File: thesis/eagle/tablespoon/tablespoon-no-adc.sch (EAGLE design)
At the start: 29 parts, among them IC1 7805DT, IC2 7805DT, IC3 TL072D, U1 ADCS7477, U2 ADCS7477

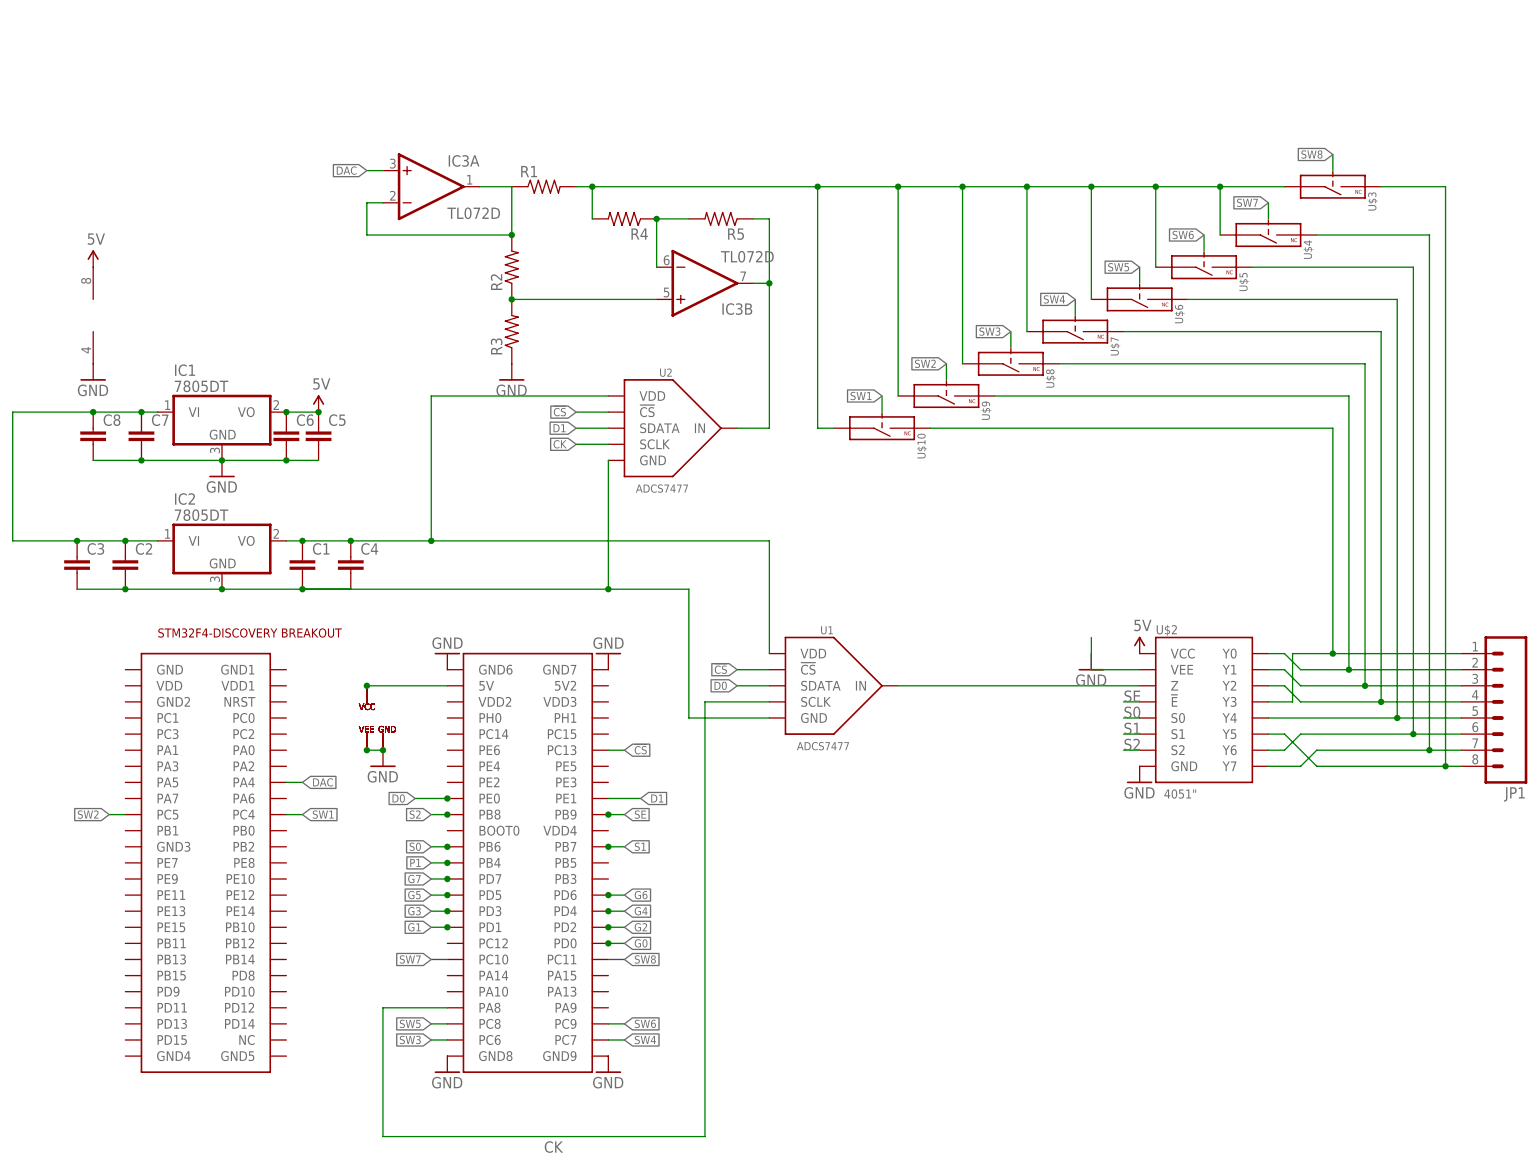
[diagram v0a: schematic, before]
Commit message: working on 8-channel DAC side
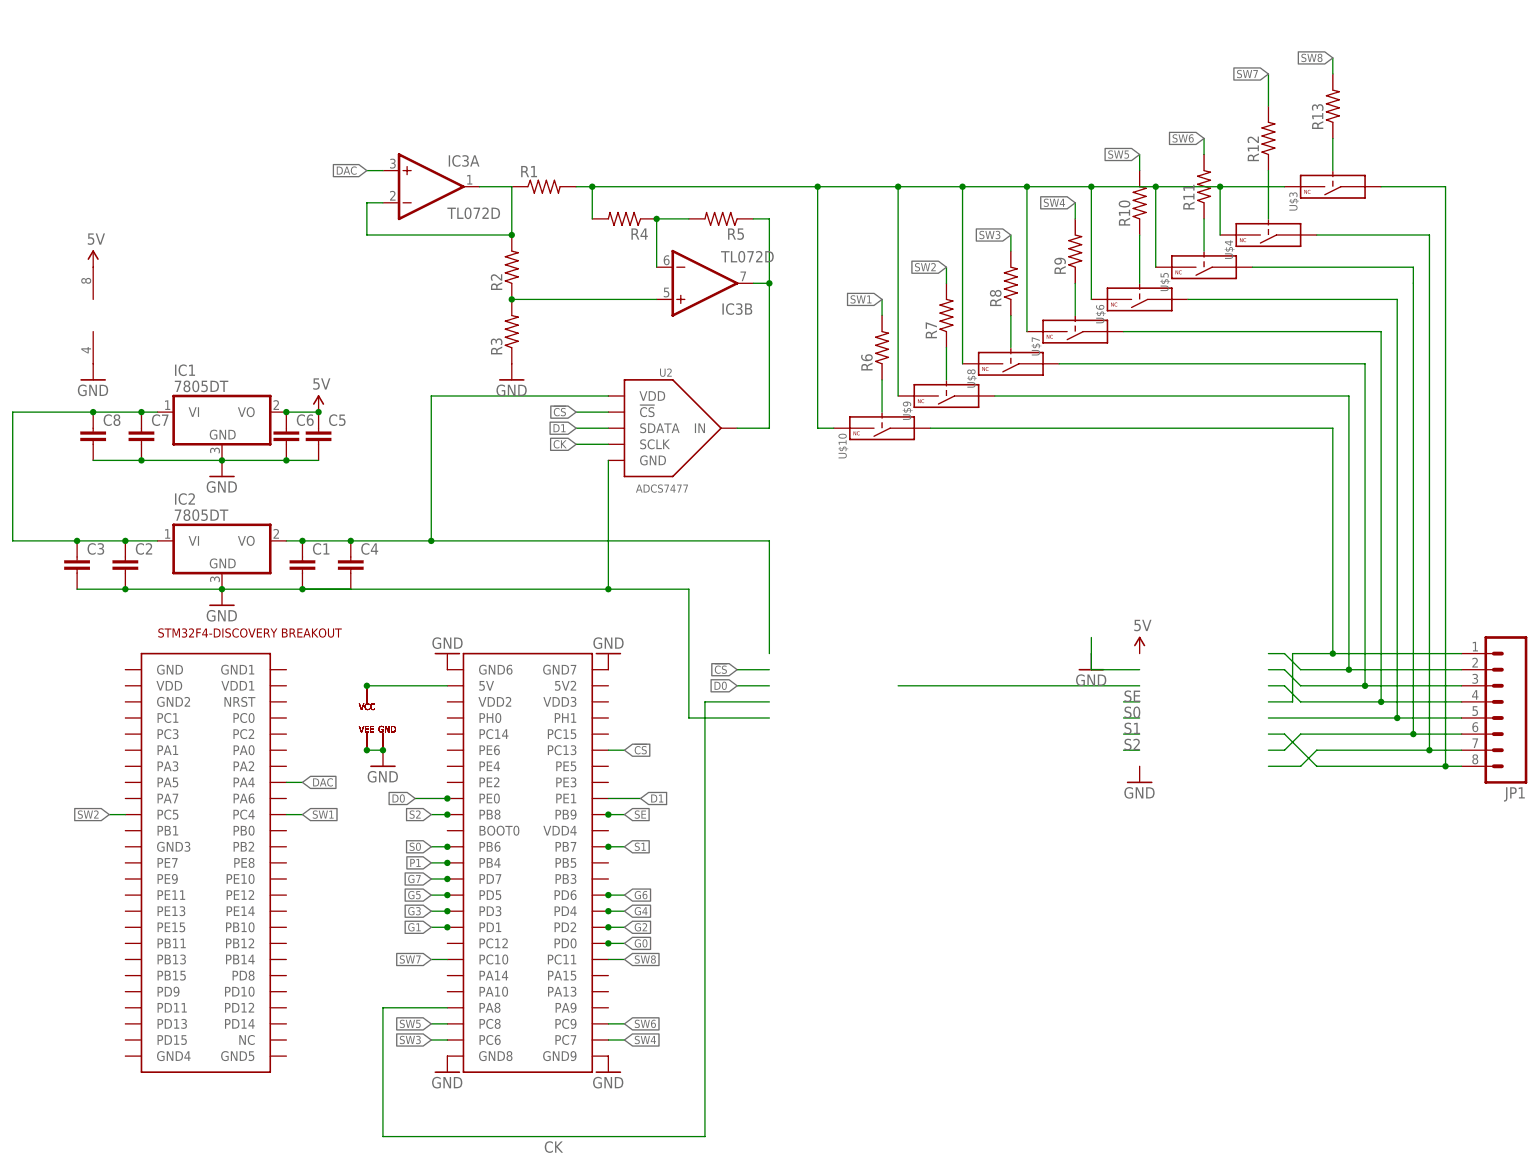
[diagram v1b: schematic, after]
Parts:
- removed U$2: 4051", butter:4051"
- removed U1: ADCS7477, butter:ADCS7477
- added R10, R11, R12, R13, R6, R7, R8, R9: (no value), SparkFun-Passives:RESISTOR0805-RES
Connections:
- net N$7 renamed 4.6V
- removed net N$1: U$2.Z, U1.IN
- removed net N$3: C1.2, C2.2, C3.2, C4.2, IC2.GND, U1.GND, U2.GND
- new net N$15: R8.1, U$8G$1.CTL
- new net N$17: R9.1, U$7G$1.CTL
- new net N$18: R12.1, U$4G$1.CTL
- new net N$19: R13.1, U$3G$1.CTL
- new net N$20: R11.1, U$5G$1.CTL
- new net N$21: R10.1, U$6G$1.CTL
- new net N$4: R6.1, U$10G$1.CTL
- new net N$7: R7.1, U$9G$1.CTL
- net !CS: no longer U1.!CS
- net 5V: no longer U$2.VCC
- net CK: no longer U1.SCLK
- net D0: no longer U1.SDATA
- net GND: now also C1.2, C2.2, C3.2, C4.2, IC2.GND, U2.GND; no longer U$2.GND, U$2.VEE
- net N$10: now also U$8G$1.COM; no longer U$2.Y1, U$8G$1.IN
- net N$11: now also U$10G$1.COM; no longer U$10G$1.IN, U$2.Y3
- net N$12: now also U$9G$1.COM; no longer U$2.Y0, U$9G$1.IN
- net N$16: now also U$10G$1.IN, U$3G$1.IN, U$4G$1.IN, U$5G$1.IN, U$6G$1.IN, U$7G$1.IN, U$8G$1.IN, U$9G$1.IN; no longer U$10G$1.COM, U$3G$1.COM, U$4G$1.COM, U$5G$1.COM, U$6G$1.COM, U$7G$1.COM, U$8G$1.COM, U$9G$1.COM
- net N$2: no longer U1.VDD
- net N$27: now also U$5G$1.COM; no longer U$2.Y6, U$5G$1.IN
- net N$28: now also U$4G$1.COM; no longer U$2.Y7, U$4G$1.IN
- net N$29: now also U$3G$1.COM; no longer U$2.Y5, U$3G$1.IN
- net N$6: now also U$7G$1.COM; no longer U$2.Y2, U$7G$1.IN
- net N$9: now also U$6G$1.COM; no longer U$2.Y4, U$6G$1.IN
- net S0: no longer U$2.S0
- net S1: no longer U$2.S1
- net S2: no longer U$2.S2
- net SE: no longer U$2.!E
- net SW1: now also R6.2; no longer U$10G$1.CTL
- net SW2: now also R7.2; no longer U$9G$1.CTL
- net SW3: now also R8.2; no longer U$8G$1.CTL
- net SW4: now also R9.2; no longer U$7G$1.CTL
- net SW5: now also R10.2; no longer U$6G$1.CTL
- net SW6: now also R11.2; no longer U$5G$1.CTL
- net SW7: now also R12.2; no longer U$4G$1.CTL
- net SW8: now also R13.2; no longer U$3G$1.CTL

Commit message: driving tablespoon
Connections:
- net !CS: now also U2.!CS
- net CK: now also U2.SCLK
- net SW1: now also R11.2, U$1.PC15; no longer R6.2, U$1.PC4
- net SW2: now also R13.2, U$1.PC14; no longer R7.2, U$1.PC5
- net SW3: now also R12.2; no longer R8.2
- net SW4: now also R10.2; no longer R9.2
- net SW5: now also R8.2; no longer R10.2
- net SW6: now also R6.2; no longer R11.2
- net SW7: now also R7.2; no longer R12.2
- net SW8: now also R9.2; no longer R13.2
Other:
- moved on the sheet: R9
